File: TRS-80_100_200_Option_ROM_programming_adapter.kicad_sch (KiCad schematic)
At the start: 6 parts

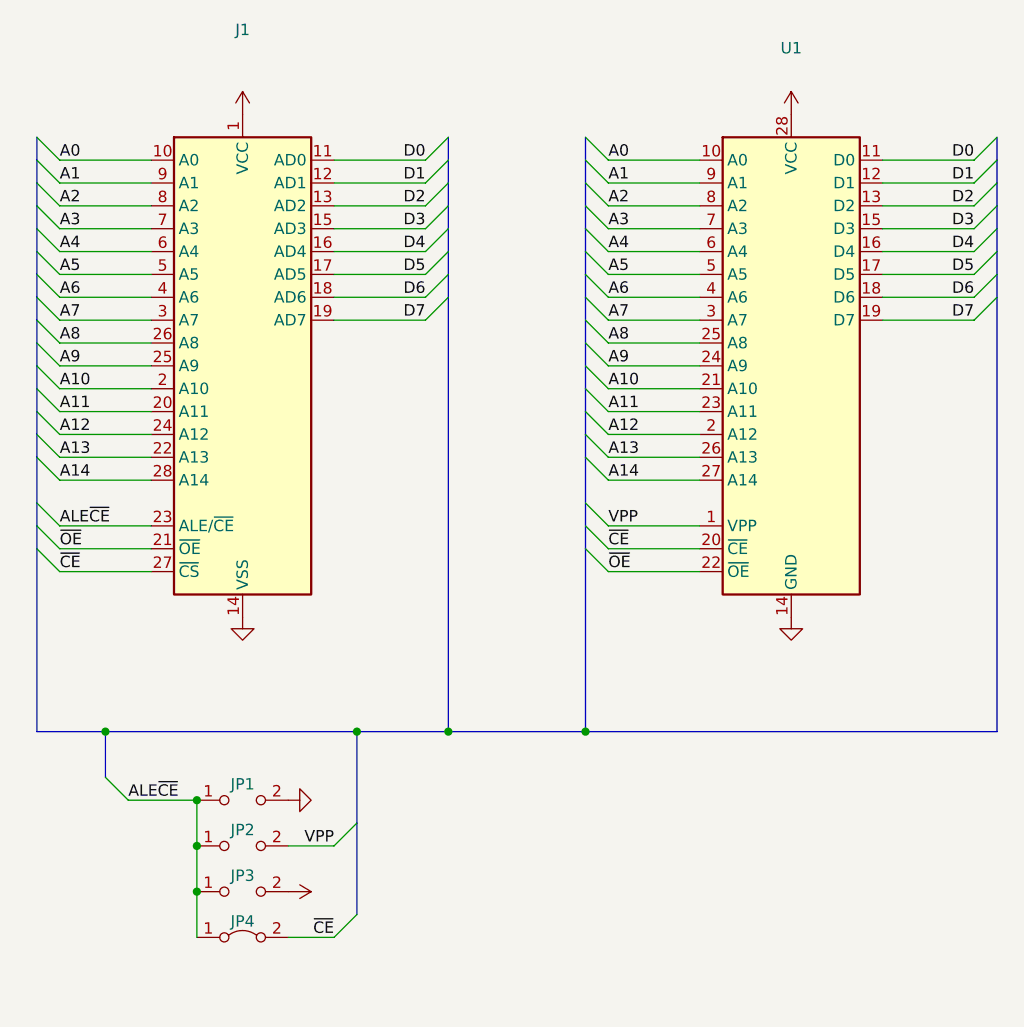
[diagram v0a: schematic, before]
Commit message: m100 optrom reader outline, silk, sch
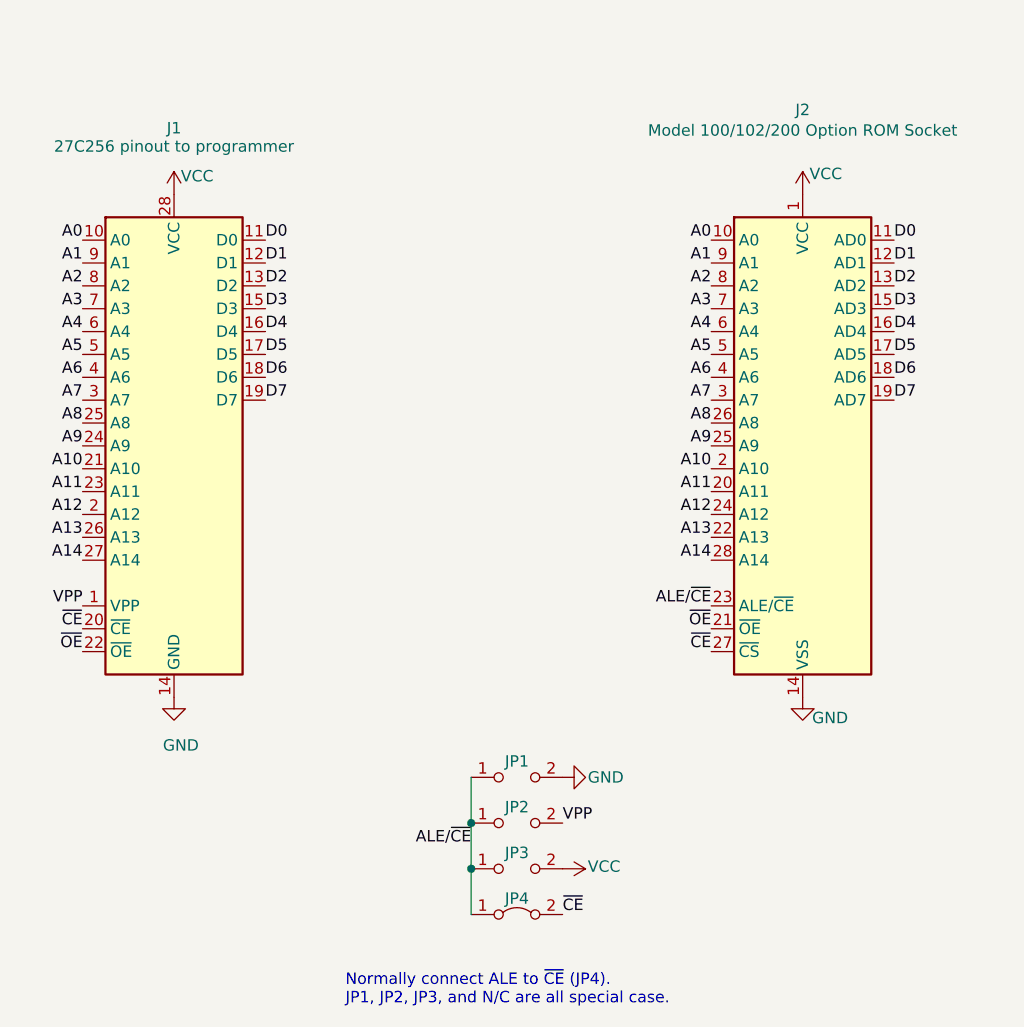
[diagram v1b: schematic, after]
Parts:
- J1: renamed from U1; value (none) -> 27C256 pinout to programmer; footprint (none) -> 000_LOCAL:2x28_0.3_0.1_pins
- J2: renamed from J1; value (none) -> Model 100/102/200 Option ROM Socket; footprint (none) -> 000_LOCAL:Molex_78805
- JP1: value (none) -> GND; footprint (none) -> 000_LOCAL:PinHeader_1x02_P2.54mm_Vertical
- JP2: value (none) -> VPP; footprint (none) -> 000_LOCAL:PinHeader_1x02_P2.54mm_Vertical
- JP3: value (none) -> VCC; footprint (none) -> 000_LOCAL:PinHeader_1x02_P2.54mm_Vertical
- JP4: value (none) -> ~{CE}; footprint (none) -> 000_LOCAL:PinHeader_1x02_P2.54mm_Vertical_shorted
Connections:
- net ALE~{CE} renamed ALE/~{CE}
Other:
- note added: "Normally connect ALE to ~{CE} (JP4). JP1, JP2, JP3, and N/C are all special case."
- moved on the sheet: J1, J2, JP1, JP2, JP3, JP4
